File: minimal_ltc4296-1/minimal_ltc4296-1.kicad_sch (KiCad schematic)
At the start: 0 parts

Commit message: Update KiCad project files (PCB layout, schematic, and project settings)
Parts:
- added U1: LTC4296AUK-1-PBF, analog_devices_footprints:QFN48_05-08-7073_ADI, symbol UNITED_IC_ADI:U_LTC4296AUK-1-PBF
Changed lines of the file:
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@@
 	(generator_version "9.0")
 	(paper "A4")
+	(symbol
+		(lib_id "UNITED_IC_ADI:U_LTC4296AUK-1-PBF")
+		(at 152.4 101.6 0)
+		(unit 1)
+		(exclude_from_sim no)
+		(in_bom yes)
+		(on_board yes)
+		(dnp no)
+		(fields_autoplaced yes)
+		(property "Reference" "U1"
+			(at 152.4 50.8 0)
+			(effects
+				(font
+					(size 1.524 1.524)
+				)
+			)
+		)
+		(property "Value" "LTC4296AUK-1-PBF"
+			(at 152.4 53.34 0)
+			(effects
+				(font
+					(size 1.524 1.524)
+				)
+			)
+		)
+		(property "Footprint" "analog_devices_footprints:QFN48_05-08-7073_ADI"
+			(at 167.64 154.94 0)
+			(effects
+				(font
+					(size 1.27 1.27)
+					(italic yes)
+				)
+				(justify left)
+				(hide yes)
+			)
+		)
+		(property "Datasheet" "https://www.analog.com/media/en/technical-documentation/data-sheets/ltc4296-1.pdf"
+			(at 167.64 149.86 0)
+			(effects
+				(font
+					(size 1.27 1.27)
+					(italic yes)
+				)
+				(justify left)
+				(hide yes)
+			)
+		)
+		(property "Description" "5-Port SPoE PSE Controller"
+			(at 167.64 152.4 0)
+			(effects
+				(font
+					(size 1.27 1.27)
+				)
+				(justify left)
+				(hide yes)
+			)
+		)
+		(property "MPN" "LTC4296AUK-1-PBF"
+			(at 167.64 157.48 0)
+			(effects
+				(font
+					(size 1.27 1.27)
+				)
+				(justify left)
+				(hide yes)
+			)
+		)
+		(pin "47"
+		)
+		(pin "22"
+		)
+		(pin "30"
+		)
+		(pin "42"
+		)
+		(pin "5"
+		)
+		(pin "39"
+		)
+		(pin "10"
+		)
+		(pin "38"
+		)
+		(pin "12"
+		)
+		(pin "13"
+		)
+		(pin "49"
+		)
+		(pin "48"
+		)
+		(pin "23"
+		)
+		(pin "41"
+		)
+		(pin "3"
+		)
+		(pin "18"
+		)
+		(pin "45"
+		)
+		(pin "27"
+		)
+		(pin "20"
+		)
+		(pin "14"
+		)
+		(pin "17"
+		)
+		(pin "2"
+		)
+		(pin "46"
+		)
+		(pin "43"
+		)
+		(pin "35"
+		)
+		(pin "19"
+		)
+		(pin "24"
+		)
+		(pin "40"
+		)
+		(pin "21"
+		)
+		(pin "37"
+		)
+		(pin "7"
+		)
+		(pin "11"
+		)
+		(pin "36"
+		)
+		(pin "4"
+		)
+		(pin "34"
+		)
+		(pin "33"
+		)
+		(pin "26"
+		)
+		(pin "6"
+		)
+		(pin "1"
+		)
+		(pin "9"
+		)
+		(pin "44"
+		)
+		(pin "8"
+		)
+		(pin "15"
+		)
+		(pin "25"
+		)
+		(pin "16"
+		)
+		(pin "28"
+		)
+		(pin "29"
+		)
+		(pin "31"
+		)
+		(pin "32"
+		)
+		(instances
+			(project ""
+				(path "/e9cd67f6-87f6-45d7-ba91-8216ce839c88"
+					(reference "U1")
+					(unit 1)
+				)
+			)
+		)
+	)
 	(sheet_instances
 		(path "/"

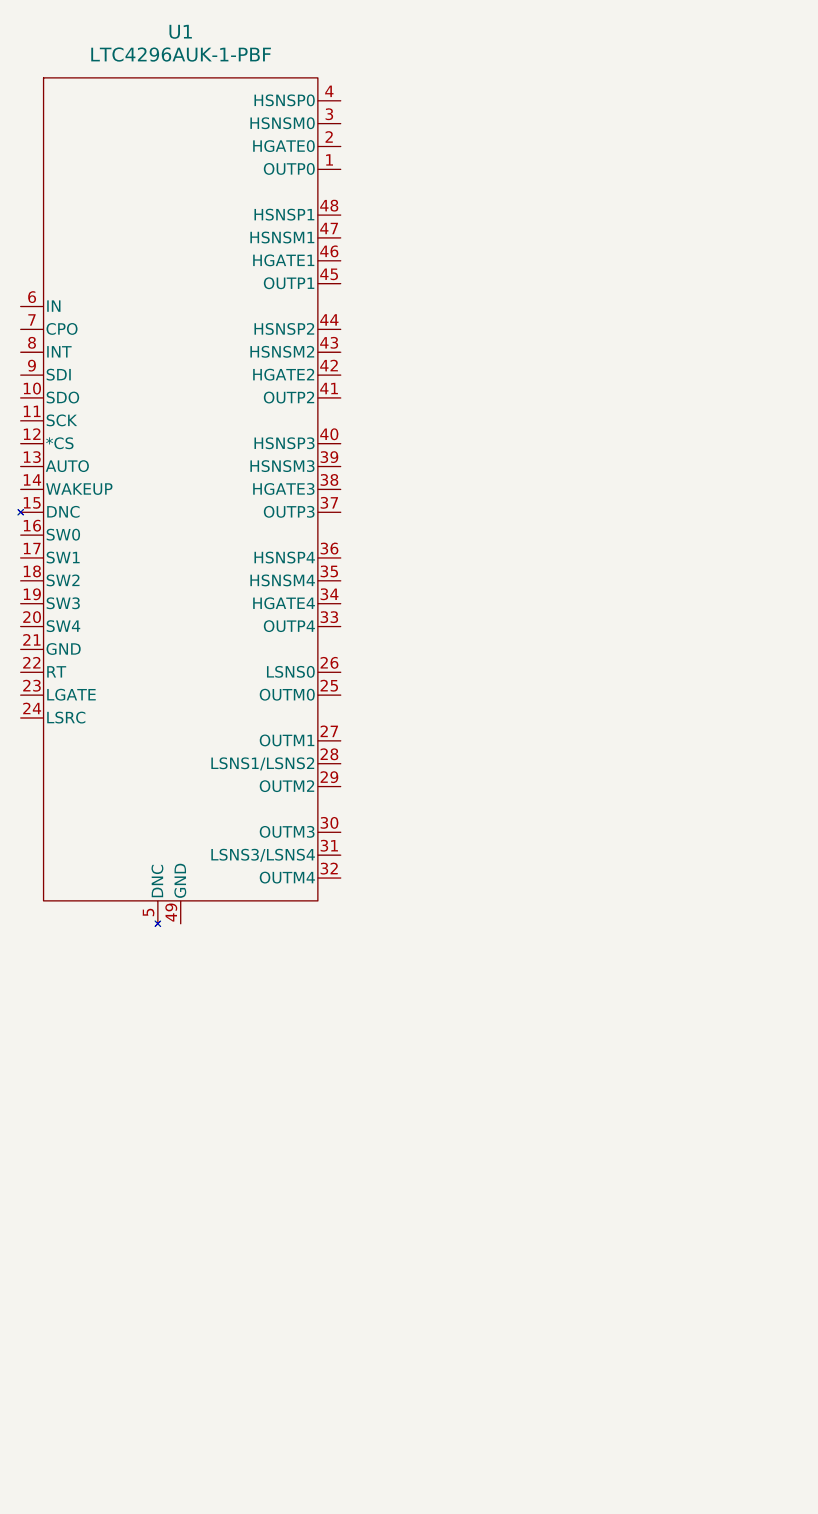
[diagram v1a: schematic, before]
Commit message: Update KiCAD project files and generator
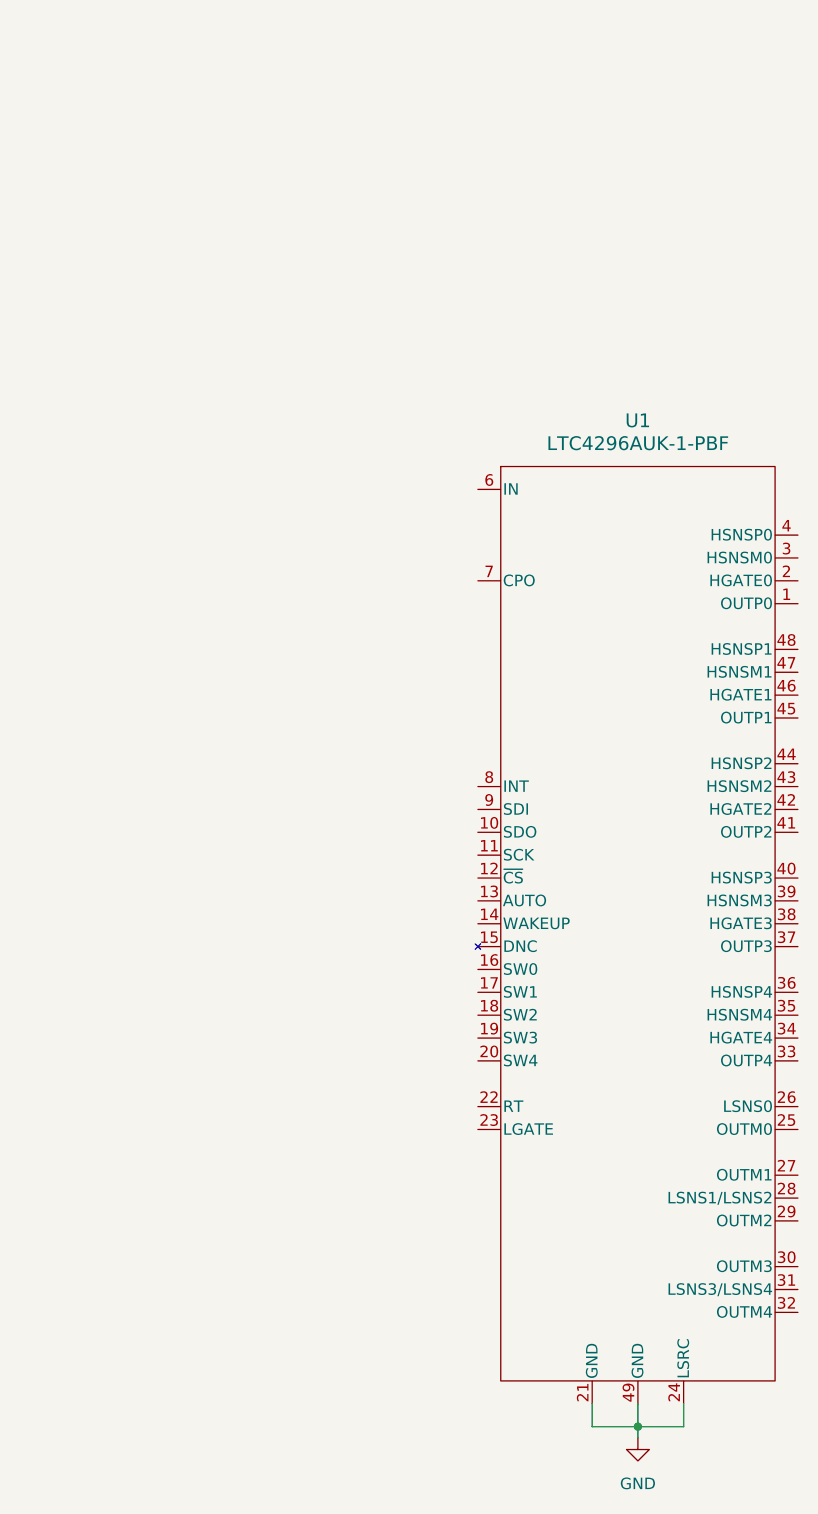
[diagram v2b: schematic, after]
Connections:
- net GND: now reaches U1.21 (GND)
- net GND: now also U1.24 (LSRC), U1.49 (GND)
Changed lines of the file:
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@@
 	(generator "eeschema")
 	(generator_version "9.0")
-	(paper "A4")
+	(paper "A3")
+	(junction
+		(at 203.2 205.74)
+		(diameter 0)
+		(color 0 0 0 0)
+	)
+	(wire
+		(pts
+			(xy 198.12 203.2) (xy 198.12 205.74)
+		)
+		(stroke
+			(width 0)
+			(type default)
+		)
+	)
+	(wire
+		(pts
+			(xy 208.28 203.2) (xy 208.28 205.74)
+		)
+		(stroke
+			(width 0)
+			(type default)
+		)
+	)
+	(wire
+		(pts
+			(xy 203.2 205.74) (xy 208.28 205.74)
+		)
+		(stroke
+			(width 0)
+			(type default)
+		)
+	)
+	(wire
+		(pts
+			(xy 203.2 203.2) (xy 203.2 205.74)
+		)
+		(stroke
+			(width 0)
+			(type default)
+		)
+	)
+	(wire
+		(pts
+			(xy 198.12 205.74) (xy 203.2 205.74)
+		)
+		(stroke
+			(width 0)
+			(type default)
+		)
+	)
+	(wire
+		(pts
+			(xy 203.2 205.74) (xy 203.2 207.01)
+		)
+		(stroke
+			(width 0)
+			(type default)
+		)
+	)
 	(symbol
 		(lib_id "UNITED_IC_ADI:U_LTC4296AUK-1-PBF")
-		(at 152.4 101.6 0)
+		(at 203.2 149.86 0)
 		(unit 1)
 		(exclude_from_sim no)
@@
 		(fields_autoplaced yes)
 		(property "Reference" "U1"
-			(at 152.4 50.8 0)
+			(at 203.2 93.98 0)
 			(effects
 				(font
@@
 		)
 		(property "Value" "LTC4296AUK-1-PBF"
-			(at 152.4 53.34 0)
+			(at 203.2 96.52 0)
 			(effects
 				(font
@@
 		)
 		(property "Footprint" "analog_devices_footprints:QFN48_05-08-7073_ADI"
-			(at 167.64 154.94 0)
+			(at 218.44 203.2 0)
 			(effects
 				(font
@@
 		)
 		(property "Datasheet" "https://www.analog.com/media/en/technical-documentation/data-sheets/ltc4296-1.pdf"
-			(at 167.64 149.86 0)
+			(at 218.44 198.12 0)
 			(effects
 				(font
@@
 		)
 		(property "Description" "5-Port SPoE PSE Controller"
-			(at 167.64 152.4 0)
+			(at 218.44 200.66 0)
 			(effects
 				(font
@@
 		)
 		(property "MPN" "LTC4296AUK-1-PBF"
-			(at 167.64 157.48 0)
+			(at 218.44 205.74 0)
 			(effects
 				(font
@@
 					(unit 1)
 				)
+			)
+		)
+	)
+	(symbol
+		(lib_id "power:GND")
+		(at 203.2 207.01 0)
+		(unit 1)
+		(exclude_from_sim no)
+		(in_bom yes)
+		(on_board yes)
+		(dnp no)
+		(fields_autoplaced yes)
+		(property "Reference" "#PWR01"
+			(at 203.2 213.36 0)
+			(effects
+				(font
+					(size 1.27 1.27)
+				)
+				(hide yes)
+			)
+		)
+		(property "Value" "GND"
+			(at 203.2 212.09 0)
+			(effects
+				(font
+					(size 1.27 1.27)
+				)
+			)
+		)
+		(property "Footprint" ""
+			(at 203.2 207.01 0)
+			(effects
+				(font
+					(size 1.27 1.27)
+				)
+				(hide yes)
+			)
+		)
+		(property "Datasheet" ""
+			(at 203.2 207.01 0)
+			(effects
+				(font
+					(size 1.27 1.27)
+				)
+				(hide yes)
+			)
+		)
+		(property "Description" "Power symbol creates a global label with name \"GND\" , ground"
+			(at 203.2 207.01 0)
+			(effects
+				(font
+					(size 1.27 1.27)
+				)
+				(hide yes)
+			)
+		)
+		(pin "1"
+		)
+		(instances
+			(project "minimal_ltc4296-1"
+				(path "/e9cd67f6-87f6-45d7-ba91-8216ce839c88"
+					(reference "#PWR01")
+					(unit 1)
+				)

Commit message: Update KiCad project files
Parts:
- added C1: 1 nF, capacitor_footprints:C_0402_1005Metric, symbol CAPACITORS_C1005X7S2A_DATA_BASE:C_C1005X7S2A102K050BB
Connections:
- net IN: now reaches U1.6 (IN)
- net IN: now also C1.1
- net CPO: now reaches U1.7 (CPO)
- net CPO: now also C1.2

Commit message: Update KiCAD files and submodule
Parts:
- added C2, C5: 100 nF, capacitor_footprints:C_0603_1608Metric, symbol CAPACITORS_C1608X7S2A_DATA_BASE:C_C1608X7S2A104K080AB
- added C3: 10 µF, capacitor_footprints:C_1210_250_3225Metric, symbol CAPACITORS_GRM32EC72A_DATA_BASE:C_GRM32EC72A106KE05L
- added C4: 470 nF, capacitor_footprints:C_0402_1005Metric, symbol CAPACITORS_C1005X5R1E_DATA_BASE:C_C1005X5R1E474K050BB
- added D1: 58 V, diode_footprints:DO-214AA, symbol DIODES_SMBJ_DATA_BASE:D_SMBJ58CA
- added R1, R3, R4: 10 kΩ, resistor_footprints:R_0402_1005Metric, symbol RESISTORS_ERJ-2RKF_DATA_BASE:R_ERJ-2RKF1002X
- added R2: 4.99 kΩ, resistor_footprints:R_0402_1005Metric, symbol RESISTORS_ERJ-2RKF_DATA_BASE:R_ERJ-2RKF4991X
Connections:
- net GND: now also C2.2, C3.2, C4.2, C5.2, D1.2
- net IN: now also C2.1, C3.1, D1.1
- net SDO: now reaches U1.10 (SDO)
- net SDO: now also R2.2
- net SCK: now reaches U1.11 (SCK)
- net SCK: now also R3.2
- net ~{CS}: now reaches U1.12 (~{CS})
- net ~{CS}: now also R4.2
- net INT: now reaches U1.8 (INT)
- net INT: now also C4.1
- net SDI: now reaches U1.9 (SDI)
- net SDI: now also R1.2
- new net 3V3: C5.1, R1.1, R2.1, R3.1, R4.1

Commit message: Update KiCAD files and submodule
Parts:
- added R5, R6: 100 kΩ, resistor_footprints:R_0402_1005Metric, symbol RESISTORS_ERJ-2RKF_DATA_BASE:R_ERJ-2RKF1003X
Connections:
- net 3V3: now also R5.1
- net GND: now also R6.2
- net AUTO: now reaches U1.13 (AUTO)
- net AUTO: now also R5.2, R6.1
- net WAKEUP: now reaches U1.14 (WAKEUP)
- net SW0: now reaches U1.16 (SW0)
- net SW1: now reaches U1.17 (SW1)
- net SW2: now reaches U1.18 (SW2)
- net SW3: now reaches U1.19 (SW3)
- net SW4: now reaches U1.20 (SW4)
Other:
- moved on the sheet: C5, R1, R2, R3, R4

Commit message: Update KiCAD project files and generator
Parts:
- added C6: 1 nF, capacitor_footprints:C_0402_1005Metric, symbol CAPACITORS_GCM155R71H_DATA_BASE:C_GCM155R71H102KA37D
- added Q1: 100.0 V, transistor_footprints:LFPAK33-8, symbol TRANSISTORS_PSMN075-100MSEX_DATA_BASE:Q_PSMN075-100MSEX
- added R7: 1 kΩ, resistor_footprints:R_0402_1005Metric, symbol RESISTORS_ERJ-2RKF_DATA_BASE:R_ERJ-2RKF1001X
- added R8: 100 kΩ, resistor_footprints:R_0402_1005Metric, symbol RESISTORS_ERJ-2RKF_DATA_BASE:R_ERJ-2RKF1003X
- added R9: 24.3 kΩ, resistor_footprints:R_0402_1005Metric, symbol RESISTORS_ERJ-2RKF_DATA_BASE:R_ERJ-2RKF2432X
- added S1: TS21-34-035-BK-160-SMT-TR, tactile_switches_footprints:TS21, symbol TACTILE_SWITCHES_TS21-34-035-BK-160-SMT-TR_DATA_BASE:S_TS21-34-035-BK-160-SMT-TR
- C5: value 100 nF -> 1 nF; footprint capacitor_footprints:C_0603_1608Metric -> capacitor_footprints:C_0402_1005Metric; symbol CAPACITORS_C1608X7S2A_DATA_BASE:C_C1608X7S2A104K080AB -> CAPACITORS_GCM155R71H_DATA_BASE:C_GCM155R71H102KA37D; Case Code - in 0603 -> 0402; Case Code - mm 1608 -> 1005; Dielectric X7S -> X7R; MPN C1608X7S2A104K080AB -> GCM155R71H102KA37D; Manufacturer TDK -> Murata Electronics; Series C1608X7S2A -> GCM155R71H; Symbol Name C_C1608X7S2A104K080AB -> C_GCM155R71H102KA37D; Trustedparts Search https://www.trustedparts.com/en/search/C1608X7S2A104K080AB -> https://www.trustedparts.com/en/search/GCM155R71H102KA37D; Voltage Rating 100V -> 50V
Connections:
- net 3V3: now also R7.1
- net GND: now also C6.1, Q1.1 (S), Q1.2 (S), Q1.3 (S), R8.1, R9.2
- net WAKEUP: now also C6.2, R8.2, S1.3, S1.4
- net RT: now reaches U1.22 (RT)
- net RT: now also R9.1
- net at U1.23 (LGATE): now also Q1.4 (G)
- new net: R7.2, S1.1, S1.2
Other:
- moved on the sheet: C5

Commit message: Update KiCAD schematic and PCB files
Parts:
- added R10: 24 mΩ, resistor_footprints:R_0612_1632Metric, symbol RESISTORS_ERJ-B2CF_DATA_BASE:R_ERJ-B2CFR024V
- added R11, R13: 62 mΩ, resistor_footprints:R_0612_1632Metric, symbol RESISTORS_PRL1632-_DATA_BASE:R_PRL1632-R062-F-T1
- added R12: 16 mΩ, resistor_footprints:R_0612_1632Metric, symbol RESISTORS_PRL1632-_DATA_BASE:R_PRL1632-R016-F-T1
- added R14: 390 mΩ, resistor_footprints:R_0612_1632Metric, symbol RESISTORS_ERJ-B2BF_DATA_BASE:R_ERJ-B2BFR39V
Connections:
- net OUTM0: now reaches U1.25 (OUTM0)
- net OUTM0: now also R14.2
- net LSNS: now reaches U1.26 (LSNS0)
- net LSNS: now also Q1.5 (D), U1.28 (LSNS1/LSNS2), U1.31 (LSNS3/LSNS4), R10.1, R11.1, R12.1, R13.1, R14.1
- net OUTM1: now reaches U1.27 (OUTM1)
- net OUTM1: now also R12.2
- net OUTM2: now reaches U1.29 (OUTM2)
- net OUTM2: now also R13.2
- net OUTM3: now reaches U1.30 (OUTM3)
- net OUTM3: now also R10.2
- net OUTM4: now reaches U1.32 (OUTM4)
- net OUTM4: now also R11.2
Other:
- moved on the sheet: Q1, R9, U1

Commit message: Update PCB and schematic files
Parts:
- added Q2: 100.0 V, transistor_footprints:LFPAK33-8, symbol TRANSISTORS_PSMN075-100MSEX_DATA_BASE:Q_PSMN075-100MSEX
- added Q3: 100.0 V, transistor_footprints:LFPAK33-8, symbol TRANSISTORS_PSMN040-100MSEX_DATA_BASE:Q_PSMN040-100MSEX
- added R15: 24 mΩ, resistor_footprints:R_0612_1632Metric, symbol RESISTORS_ERJ-B2CF_DATA_BASE:R_ERJ-B2CFR024V
- added R16: 390 mΩ, resistor_footprints:R_0612_1632Metric, symbol RESISTORS_ERJ-B2BF_DATA_BASE:R_ERJ-B2BFR39V
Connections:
- net IN is gone; now on net PSE: C1.1, C2.1, C3.1, D1.1, U1.6 (IN)
- net GND: now also Q1.4 (G), U1.23 (LGATE)
- net OUTP4: now reaches U1.33 (OUTP4)
- net OUTP4: now also Q2.1 (S), Q2.2 (S), Q2.3 (S)
- net HGATE4: now reaches U1.34 (HGATE4)
- net HGATE4: now also Q2.4 (G)
- net HSNSM4: now reaches U1.35 (HSNSM4)
- net HSNSM4: now also Q2.5 (D), R15.2
- net PSE: now reaches U1.36 (HSNSP4)
- net PSE: now also U1.40 (HSNSP3), R15.1, R16.1
- net OUTP3: now reaches U1.37 (OUTP3)
- net OUTP3: now also Q3.1 (S), Q3.2 (S), Q3.3 (S)
- net HGATE3: now reaches U1.38 (HGATE3)
- net HGATE3: now also Q3.4 (G)
- net HSNSM3: now reaches U1.39 (HSNSM3)
- net HSNSM3: now also Q3.5 (D), R16.2
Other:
- moved on the sheet: C1, C2, C3, C4, C5, C6, D1, Q1, R1, R10, R11, R12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
